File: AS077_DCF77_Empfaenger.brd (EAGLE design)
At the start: 160 x 100 mm, 82 parts, among them IC1 4093N, IC2 4538N, IC3 CA3130E, IC4 4093N, J1 Rückkopplung, J2 JUMPER_J5MM, J3 JUMPER_J5MM, Q1 BF244A, Q2 BC549C, Q3 BC549C, Q4 BC549C, Q5 BC549C, Q6 BC559C, Q7 BC549C

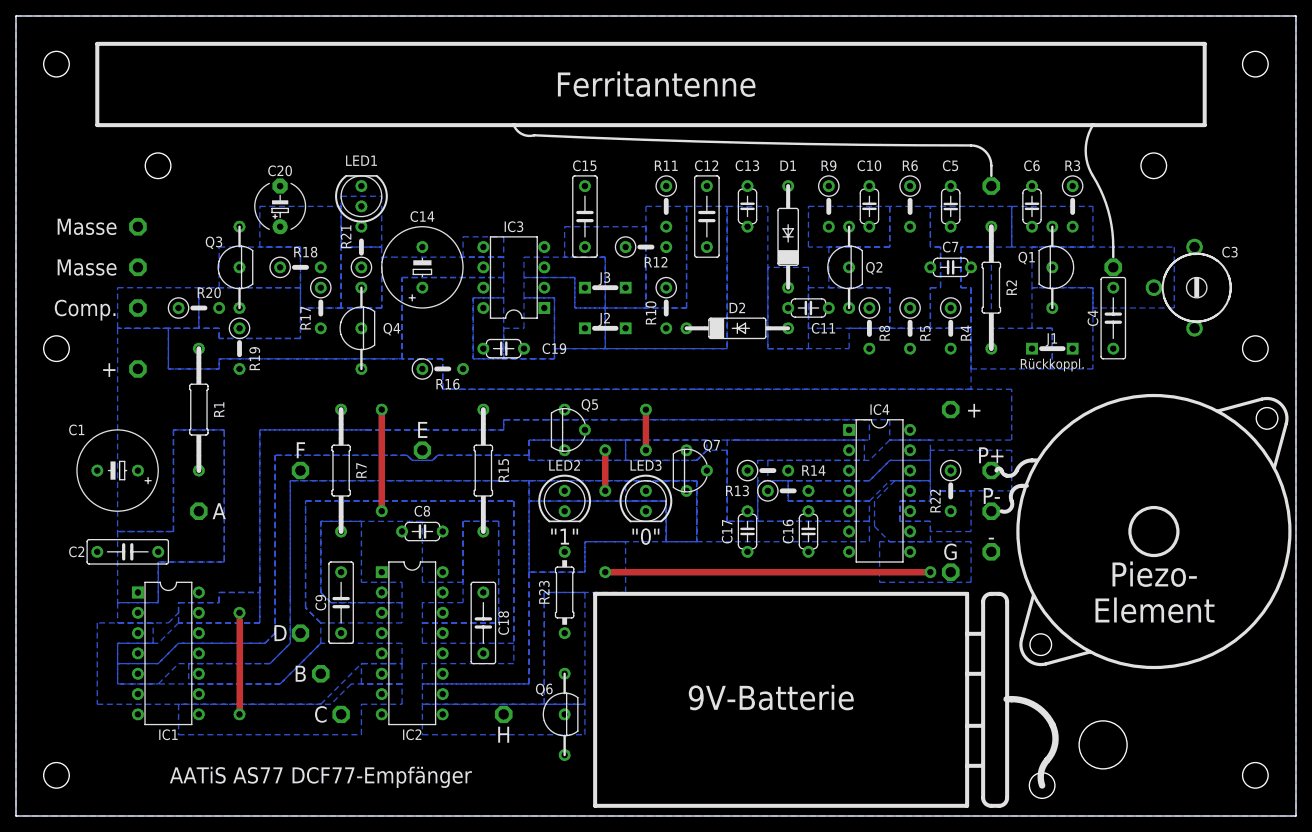
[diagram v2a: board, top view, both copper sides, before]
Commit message: * more silkscreen improvements * added GERBER
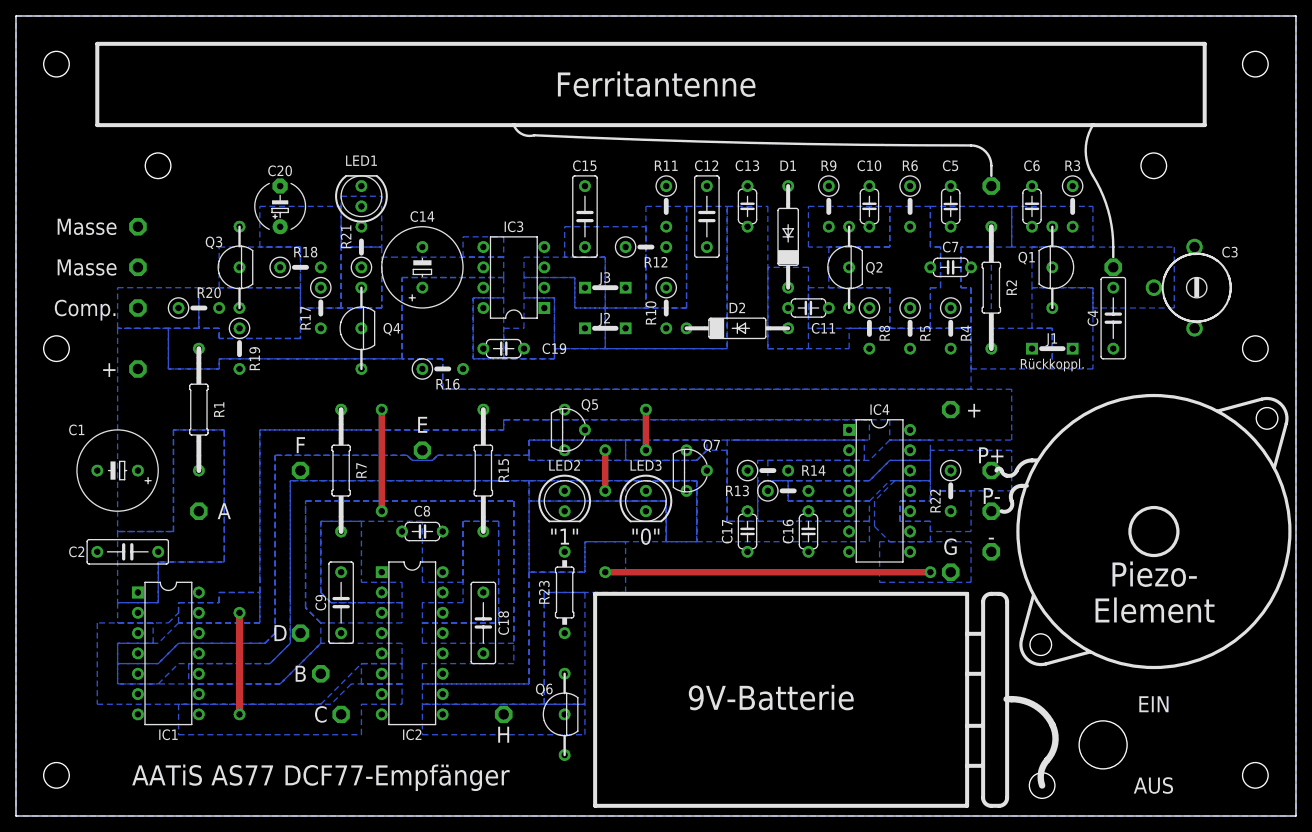
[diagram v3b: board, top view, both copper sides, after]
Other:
- board text added: "AUS"
- board text added: "EIN"
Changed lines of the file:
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@@
 <grid distance="0.635" unitdist="mm" unit="mm" style="dots" multiple="1" display="yes" altdistance="0.05" altunitdist="mm" altunit="mm"/>
 <layers>
-<layer number="1" name="Top" color="4" fill="1" visible="no" active="yes"/>
+<layer number="1" name="Top" color="4" fill="1" visible="yes" active="yes"/>
 <layer number="2" name="Route2" color="1" fill="3" visible="no" active="no"/>
 <layer number="3" name="Route3" color="4" fill="3" visible="no" active="no"/>
@@
 <layer number="14" name="Route14" color="1" fill="6" visible="no" active="no"/>
 <layer number="15" name="Route15" color="4" fill="6" visible="no" active="no"/>
-<layer number="16" name="Bottom" color="1" fill="1" visible="yes" active="yes"/>
+<layer number="16" name="Bottom" color="1" fill="1" visible="no" active="yes"/>
 <layer number="17" name="Pads" color="2" fill="1" visible="yes" active="yes"/>
 <layer number="18" name="Vias" color="2" fill="1" visible="yes" active="yes"/>
 <layer number="19" name="Unrouted" color="6" fill="1" visible="yes" active="yes"/>
 <layer number="20" name="Dimension" color="15" fill="1" visible="yes" active="yes"/>
-<layer number="21" name="tPlace" color="7" fill="1" visible="no" active="yes"/>
+<layer number="21" name="tPlace" color="7" fill="1" visible="yes" active="yes"/>
 <layer number="22" name="bPlace" color="7" fill="1" visible="yes" active="yes"/>
-<layer number="23" name="tOrigins" color="15" fill="1" visible="no" active="yes"/>
-<layer number="24" name="bOrigins" color="15" fill="1" visible="yes" active="yes"/>
-<layer number="25" name="tNames" color="7" fill="1" visible="no" active="yes"/>
-<layer number="26" name="bNames" color="7" fill="1" visible="yes" active="yes"/>
+<layer number="23" name="tOrigins" color="15" fill="1" visible="yes" active="yes"/>
+<layer number="24" name="bOrigins" color="15" fill="1" visible="no" active="yes"/>
+<layer number="25" name="tNames" color="7" fill="1" visible="yes" active="yes"/>
+<layer number="26" name="bNames" color="7" fill="1" visible="no" active="yes"/>
 <layer number="27" name="tValues" color="7" fill="1" visible="no" active="yes"/>
 <layer number="28" name="bValues" color="7" fill="1" visible="no" active="yes"/>
@@
 <layer number="37" name="tTest" color="7" fill="1" visible="no" active="yes"/>
 <layer number="38" name="bTest" color="7" fill="1" visible="no" active="yes"/>
-<layer number="39" name="tKeepout" color="4" fill="11" visible="no" active="yes"/>
-<layer number="40" name="bKeepout" color="1" fill="11" visible="yes" active="yes"/>
-<layer number="41" name="tRestrict" color="4" fill="10" visible="no" active="yes"/>
-<layer number="42" name="bRestrict" color="1" fill="10" visible="yes" active="yes"/>
+<layer number="39" name="tKeepout" color="4" fill="11" visible="yes" active="yes"/>
+<layer number="40" name="bKeepout" color="1" fill="11" visible="no" active="yes"/>
+<layer number="41" name="tRestrict" color="4" fill="10" visible="yes" active="yes"/>
+<layer number="42" name="bRestrict" color="1" fill="10" visible="no" active="yes"/>
 <layer number="43" name="vRestrict" color="2" fill="10" visible="no" active="yes"/>
 <layer number="44" name="Drills" color="7" fill="1" visible="no" active="yes"/>
@@
 <layer number="49" name="Reference" color="7" fill="1" visible="no" active="yes"/>
 <layer number="50" name="dxf" color="7" fill="1" visible="no" active="no"/>
-<layer number="51" name="tDocu" color="7" fill="1" visible="no" active="yes"/>
-<layer number="52" name="bDocu" color="7" fill="1" visible="yes" active="yes"/>
+<layer number="51" name="tDocu" color="7" fill="1" visible="yes" active="yes"/>
+<layer number="52" name="bDocu" color="7" fill="1" visible="no" active="yes"/>
 <layer number="56" name="wert" color="7" fill="1" visible="no" active="no"/>
 <layer number="88" name="SimResults" color="9" fill="1" visible="no" active="no"/>
@@
 <wire x1="109.835" y1="41.91" x2="109.2" y2="41.91" width="0.8128" layer="42"/>
 <hole x="135.89" y="8.89" drill="6"/>
-<text x="38.1" y="5.08" size="2" layer="21" font="vector" ratio="15" align="center">AATiS AS77 DCF77-Empfänger</text>
+<text x="38.1" y="5.08" size="2.5" layer="21" font="vector" ratio="15" align="center">AATiS AS77 DCF77-Empfänger</text>
 <text x="5.08" y="16.51" size="2.5" layer="30" font="vector" ratio="15" rot="MR90" align="center">DK2ZA</text>
 <hole x="128.27" y="3.81" drill="3.2"/>
@@
 <text x="68.58" y="34.925" size="2" layer="21" font="vector" ratio="15" align="center">"1"</text>
 <text x="78.74" y="34.925" size="2" layer="21" font="vector" ratio="15" align="center">"0"</text>
-<text x="116.84" y="33.02" size="2" layer="21" font="vector" ratio="15" align="center">G</text>
+<text x="116.84" y="33.655" size="2" layer="21" font="vector" ratio="15" align="center">G</text>
 <text x="118.745" y="50.8" size="2" layer="21" font="vector" ratio="15" align="center-left">+</text>
 <text x="121.92" y="45.085" size="2" layer="21" font="vector" ratio="15" align="center">P+</text>
@@
 <text x="121.92" y="34.925" size="2" layer="21" font="vector" ratio="15" align="center">-</text>
 <text x="60.96" y="10.16" size="2" layer="21" font="vector" ratio="15" align="center">H</text>
-<text x="25.4" y="38.1" size="2" layer="21" font="vector" ratio="15" align="center">A</text>
-<text x="35.56" y="45.72" size="2" layer="21" font="vector" ratio="15" align="center">F</text>
-<text x="50.8" y="48.26" size="2" layer="21" font="vector" ratio="15" align="center">E</text>
+<text x="26.035" y="38.1" size="2" layer="21" font="vector" ratio="15" rot="R180" align="center">A</text>
+<text x="35.56" y="46.355" size="2" layer="21" font="vector" ratio="15" align="center">F</text>
+<text x="50.8" y="48.895" size="2" layer="21" font="vector" ratio="15" align="center">E</text>
 <wire x1="10.16" y1="96.52" x2="148.59" y2="96.52" width="0.5" layer="21"/>
 <wire x1="148.59" y1="96.52" x2="148.59" y2="86.36" width="0.5" layer="21"/>
@@
 <wire x1="64.77" y1="85.09" x2="62.23" y2="86.36" width="0.3" layer="21" curve="-84.671157"/>
 <wire x1="1.27" y1="53.34" x2="158.75" y2="53.34" width="0.3" layer="22" style="longdash"/>
-<text x="102.87" y="5.08" size="1.5" layer="22" font="vector" ratio="10" rot="MR0" align="center">https://github.com/SebiR</text>
+<text x="42.545" y="5.08" size="2" layer="22" font="vector" ratio="12" rot="MR0" align="center">https://github.com/SebiR</text>
 <text x="146.05" y="55.88" size="1.5" layer="22" font="vector" ratio="10" rot="MR0" align="center">Analog</text>
 <text x="146.05" y="50.8" size="1.5" layer="22" font="vector" ratio="10" rot="MR0" align="center">Digital</text>
@@
 <text x="118.11" y="50.8" size="2" layer="22" font="vector" ratio="15" rot="MR180" align="center-left">BAT+</text>
 <text x="123.19" y="33.02" size="2" layer="22" font="vector" ratio="15" rot="MR180" align="center-left">BAT-</text>
+<text x="142.24" y="3.81" size="2" layer="21" font="vector" ratio="15" align="center">AUS</text>
+<text x="142.24" y="13.97" size="2" layer="21" font="vector" ratio="15" align="center">EIN</text>
 </plain>
 <attributes>

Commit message: * Updated and cleaned up the library * Cleaned up the schematic * Renumbered all parts * Updated images, gerbers and schematic pdf * Added small arduino test script for decoding
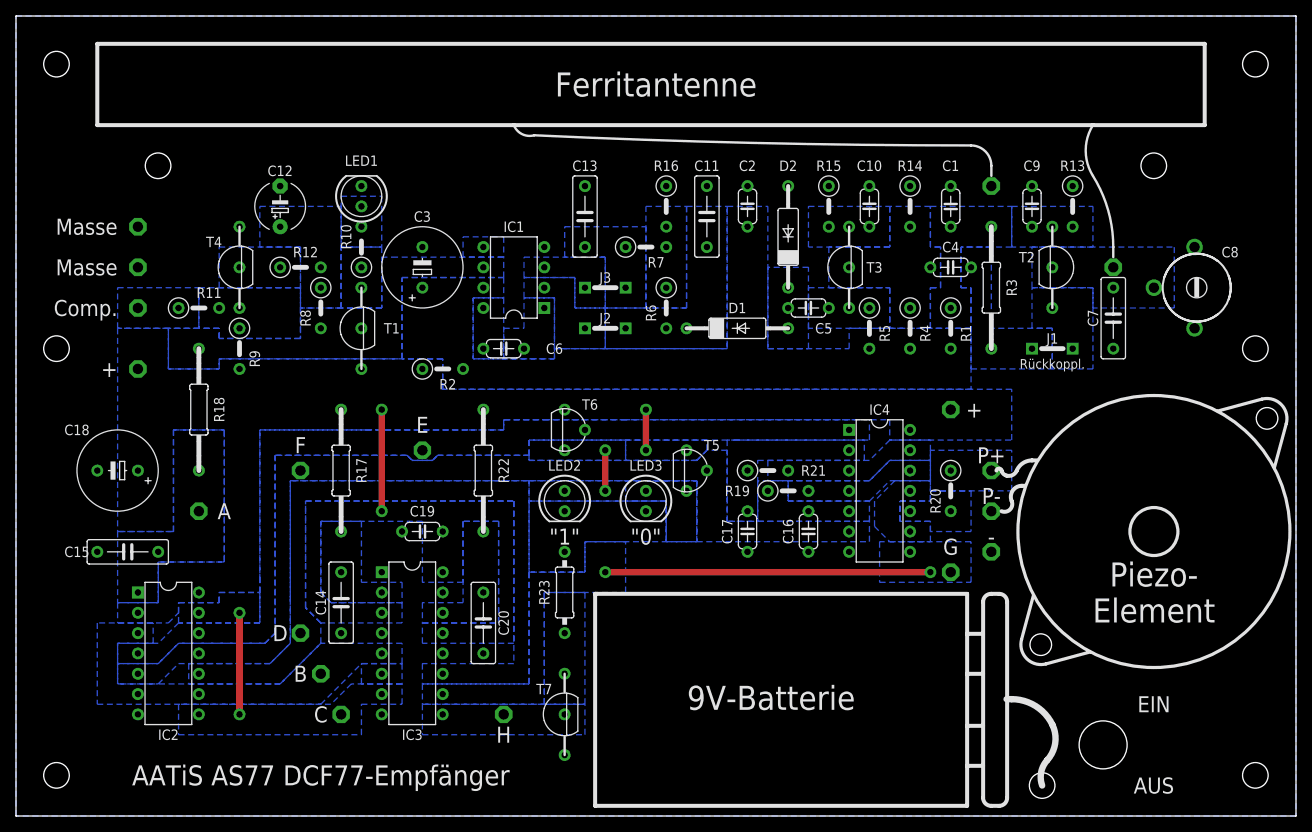
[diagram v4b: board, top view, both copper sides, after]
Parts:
- removed PAD144, PAD8463: F, 0027 DCF77-Empfänger:WIREPAD_2.2/1.3
- removed U$2: (no value), 0027 DCF77-Empfänger:34MM_PIEZO_SCREW
- added PAD17: H, 0027 DCF77-Empfänger:WIREPAD_2.2/1.3
- added PAD18: G, 0027 DCF77-Empfänger:WIREPAD_2.2/1.3
- added T2: BF244A, 0027 DCF77-Empfänger:TO92_5.08
- C1: value 470u -> 100n; device 0027 DCF77-Empfänger:RCL_E5-10,5 -> 0027 DCF77-Empfänger:RCL_C050-024X044
- C11, C13: value 100n -> 270n*; device 0027 DCF77-Empfänger:RCL_C050-024X044 -> 0027 DCF77-Empfänger:RCL_C075-032X103
- C12: value 270n* -> 1µ; device 0027 DCF77-Empfänger:RCL_C075-032X103 -> 0027 DCF77-Empfänger:E5-6
- C14: value 470u -> 150n*; device 0027 DCF77-Empfänger:RCL_E5-10,5 -> 0027 DCF77-Empfänger:RCL_C075-032X103
- C18: value 470n* -> 470u; device 0027 DCF77-Empfänger:RCL_C075-032X103 -> 0027 DCF77-Empfänger:RCL_E5-10,5
- C19: value 150p -> 100n
- C2: value 270n* -> 100n; device 0027 DCF77-Empfänger:RCL_C075-032X103 -> 0027 DCF77-Empfänger:RCL_C050-024X044
- C20: value 1µ -> 470n*; device 0027 DCF77-Empfänger:E5-6 -> 0027 DCF77-Empfänger:RCL_C075-032X103
- C3: value 90p -> 470u; device 0027 DCF77-Empfänger:RCL_CTRIM808-BC7.5 -> 0027 DCF77-Empfänger:RCL_E5-10,5
- C4: value 1n2..2n2* -> 10n; device 0027 DCF77-Empfänger:RCL_C075-032X103 -> 0027 DCF77-Empfänger:RCL_C050-024X044
- C6: value 100n -> 150p
- C7: value 10n -> 1n2..2n2*; device 0027 DCF77-Empfänger:RCL_C050-024X044 -> 0027 DCF77-Empfänger:RCL_C075-032X103
- C8: value 100n -> 90p; device 0027 DCF77-Empfänger:RCL_C050-024X044 -> 0027 DCF77-Empfänger:RCL_CTRIM808-BC7.5
- C9: value 150n* -> 100n; device 0027 DCF77-Empfänger:RCL_C075-032X103 -> 0027 DCF77-Empfänger:RCL_C050-024X044
- IC1: value 4093N -> CA3130E; device 0027 DCF77-Empfänger:40XX_DIL14 -> 0027 DCF77-Empfänger:DIL08
- IC2: value 4538N -> 4093N; device 0027 DCF77-Empfänger:45XX_DIL16 -> 0027 DCF77-Empfänger:DIL14
- IC3: value CA3130E -> 4538N; device 0027 DCF77-Empfänger:LINEAR_DIL08 -> 0027 DCF77-Empfänger:DIL16
- IC4: device 0027 DCF77-Empfänger:40XX_DIL14 -> 0027 DCF77-Empfänger:DIL14
- PAD1: value BAT+ -> VCC
- PAD10: value H -> BUZ+
- PAD11: value G -> BAT+
- PAD12: value VCC -> F
- PAD13: value Comp. -> E
- PAD14: value GND -> BAT-
- PAD15: value BUZ- -> GND
- PAD16: value BUZ+ -> D
- PAD2: value BAT- -> ANT
- PAD3: value ANT -> Comp.
- PAD5: value A -> GND
- PAD6: value GND -> A
- PAD9: value D -> BUZ-
- Q1: value BF244A -> 34MM_PIEZO; device 0027 DCF77-Empfänger:TO92_5.08 -> 0027 DCF77-Empfänger:34MM_PIEZO_SCREW
- R1: value 39k -> 1k; device 0027 DCF77-Empfänger:RCL_0207/15 -> 0027 DCF77-Empfänger:RCL_0207/5V
- R10: value 56k -> 1k
- R11: value 220k -> 1k
- R12: value 3M9 -> 22k
- R13, R5: value 100k -> 2k2
- R14: value 56k -> 47k
- R15: value 1M -> 1k; device 0027 DCF77-Empfänger:RCL_0207/15 -> 0027 DCF77-Empfänger:RCL_0207/5V
- R16: value 2k2 -> 220k
- R17: value 22k -> 1M; device 0027 DCF77-Empfänger:RCL_0207/5V -> 0027 DCF77-Empfänger:RCL_0207/15
- R18: value 22k -> 39k; device 0027 DCF77-Empfänger:RCL_0207/5V -> 0027 DCF77-Empfänger:RCL_0207/15
- R19: value 10k -> 100k
- R2: value 3k9 -> 2k2; device 0027 DCF77-Empfänger:RCL_0207/15 -> 0027 DCF77-Empfänger:RCL_0207/5V
- R21: value 1k -> 56k
- R22: value 1k -> 1M; device 0027 DCF77-Empfänger:RCL_0207/5V -> 0027 DCF77-Empfänger:RCL_0207/15
- R3: value 2k2 -> 3k9; device 0027 DCF77-Empfänger:RCL_0207/5V -> 0027 DCF77-Empfänger:RCL_0207/15
- R4: value 1k -> 100k
- R6: value 47k -> 56k
- R7: value 1M -> 3M9; device 0027 DCF77-Empfänger:RCL_0207/15 -> 0027 DCF77-Empfänger:RCL_0207/5V
- R8: value 2k2 -> 22k
- R9: value 1k -> 10k
- moved PAD3 122.0 mm to (15.2, 63.5)
- moved PAD14 112.5 mm to (121.9, 33.0)
- moved PAD15 112.5 mm to (15.2, 73.7)
- moved C1 109.2 mm to (116.8, 76.2), turned to 270 degrees
- moved PAD1 101.7 mm to (15.2, 55.9)
- moved C8 101.2 mm to (147.3, 66.0), turned to 90 degrees
- moved C9 99.6 mm to (127.0, 76.2)
- moved R20 96.7 mm to (116.8, 40.6), turned to 270 degrees
- moved C3 96.6 mm to (50.8, 68.6)
- moved R1 94.5 mm to (116.8, 61.0)
- moved PAD16 88.7 mm to (35.6, 22.9)
- moved C2 88.7 mm to (91.4, 76.2), turned to 90 degrees
- moved PAD9 87.7 mm to (121.9, 38.1)
- moved R9 75.8 mm to (27.9, 58.4)
- moved C15 70.9 mm to (14.0, 33.0), turned to 180 degrees
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- renumbered Q2 to T3, Q3 to T4, Q4 to T1, Q5 to T6, Q6 to T7, Q7 to T5
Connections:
- net DIGITALTEIL: now also IC1.6, R18.1, R8.2; no longer IC3.6, R1.1, R17.2
- net GND: now also C1.1, C11.2, C12.-, C14.1, C18.-, C19.1, C20.1, C3.-, C7.2, C8.3, C9.2, D2.A, IC1.4, IC2.7, IC3.1, IC3.12, IC3.15, IC3.8, PAD5.1, PAD9.1, R13.1, R14.1, R15.1, R16.1, T4.3, T7.1; no longer C1.-, C12.2, C14.-, C18.1, C20.-, C3.1, C3.3, C4.2, C5.1, C6.2, C9.1, D1.A, IC1.7, IC2.1, IC2.12, IC2.15, IC2.4, IC2.8, PAD2.1, PAD6.1, R11.1, R3.1, R6.1, R9.1, T4.1, T7.3
- net N$1: now also IC1.3; no longer IC3.3
- net N$10: now also C4.2, R14.2, R4.1; no longer C7.2, R5.1, R6.2
- net N$11: now also C2.1, C3.+, IC1.7, R1.2, R2.2; no longer C13.1, C14.+, IC3.7, R16.2, R8.2
- net N$12: now also C1.2, R1.1, R3.1; no longer C5.2, R2.1, R4.1
- net N$13: now also C4.1, R3.2; no longer C7.1, R2.2
- net N$14: now also T2.3; no longer Q1.1
- net N$15: now also C9.1, R13.2, T2.1; no longer C6.1, Q1.3, R3.2
- net N$16: now also C6.2, IC1.1; no longer C19.2, IC3.1
- net N$17: now also PAD10.1, R20.1; no longer PAD16.1, R22.1
- net N$18: now also C7.1, C8.2, PAD2.1, T2.2; no longer C3.2, C4.1, PAD3.1, Q1.2
- net N$19: now also C20.2, IC3.14, R22.2; no longer C18.2, IC2.14, R15.2
- net N$2: now also IC1.2; no longer IC3.2
- net N$20: now also C12.+, R12.2, R8.1; no longer C20.+, R17.1, R18.2
- net N$21: now also PAD3.1, R11.1; no longer PAD13.1, R20.1
- net N$22: now also R12.1; no longer R18.1
- net N$23: now also R11.2, R9.1, T4.1; no longer R19.1, R20.2, T4.3
- net N$24: now also R10.2; no longer R21.2
- net N$25: now also R10.1, T1.3; no longer R21.1, T1.1
- net N$26: now also C15.1, IC2.1, PAD6.1, R18.2; no longer C2.1, IC1.1, PAD5.1, R1.2
- net N$27: now also IC2.13, IC2.8, IC3.7; no longer IC1.13, IC1.8, IC2.7
- net N$28: now also IC2.11, IC2.5, PAD12.1; no longer IC1.11, IC1.5, PAD144.1
- net N$29: now also R19.2; no longer R13.2
- net N$3: now also C13.1, R7.1; no longer C15.1, R12.1
- net N$30: now also IC2.3, IC2.6, IC2.9, IC3.5; no longer IC1.3, IC1.6, IC1.9, IC2.5
- net N$31: now also IC2.10, IC3.11, PAD16.1; no longer IC1.10, IC2.11, PAD9.1
- net N$32: now also IC2.12, IC2.4, PAD13.1; no longer IC1.12, IC1.4, PAD8463.1
- net N$33: now also R21.2; no longer R14.2
- net N$35: now also R19.1; no longer R13.1
- net N$36: now also R21.1; no longer R14.1
- net N$37: now also C14.2, IC3.2, R17.2; no longer C9.2, IC2.2, R7.2
- net N$38: now also IC3.10, PAD18.1; no longer IC2.10, PAD11.1
- net N$39: now also IC3.9, PAD17.1; no longer IC2.9, PAD10.1
- net N$4: now also R16.2, R6.1, R7.2; no longer R10.1, R11.2, R12.2
- net N$40: now also T7.3; no longer T7.1
- net N$41: now also T6.3; no longer T6.1
- net N$42: now also T5.3; no longer T5.1
- net N$44: now also R20.2; no longer R22.2
- net N$45: now also IC3.6; no longer IC2.6
- net N$46: now also IC1.5; no longer IC3.5
- net N$5: now also C11.1, D1.C, R6.2; no longer C12.1, D2.C, R10.2
- net N$6: now also C5.2, D1.A, D2.C; no longer C11.2, D1.C, D2.A
- net N$7: now also C6.1, IC1.8; no longer C19.1, IC3.8
- net N$8: now also R15.2, T3.3; no longer R9.2, T3.1
- net N$9: now also C5.1, R5.1, T3.1; no longer C11.1, R8.1, T3.3
- net VCC: now also C18.+, C19.2, IC2.14, IC2.2, IC3.13, IC3.16, IC3.3, PAD11.1, R17.1, R2.1, R22.1, R9.2, T1.1, T5.1, T6.1; no longer C1.+, C8.2, IC1.14, IC1.2, IC2.13, IC2.16, IC2.3, PAD12.1, R15.1, R16.1, R19.2, R7.1, T1.3, T5.3, T6.3
